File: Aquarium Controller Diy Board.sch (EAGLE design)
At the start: 16 parts

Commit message: 2
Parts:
- added U$1: OLED128X64, Saleem_lib:OLED128X64
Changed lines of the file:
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@@
 <part name="U$10" library="Saleem_lib" deviceset="2PIN" device=""/>
 <part name="U$11" library="Saleem_lib" deviceset="2PIN" device=""/>
+<part name="U$1" library="Saleem_lib" deviceset="OLED128X64" device=""/>
 </parts>
 <sheets>
@@
 <instance part="U$10" gate="G$1" x="139.7" y="17.78"/>
 <instance part="U$11" gate="G$1" x="154.94" y="17.78"/>
+<instance part="U$1" gate="G$1" x="111.76" y="71.12"/>
 </instances>
 <busses>

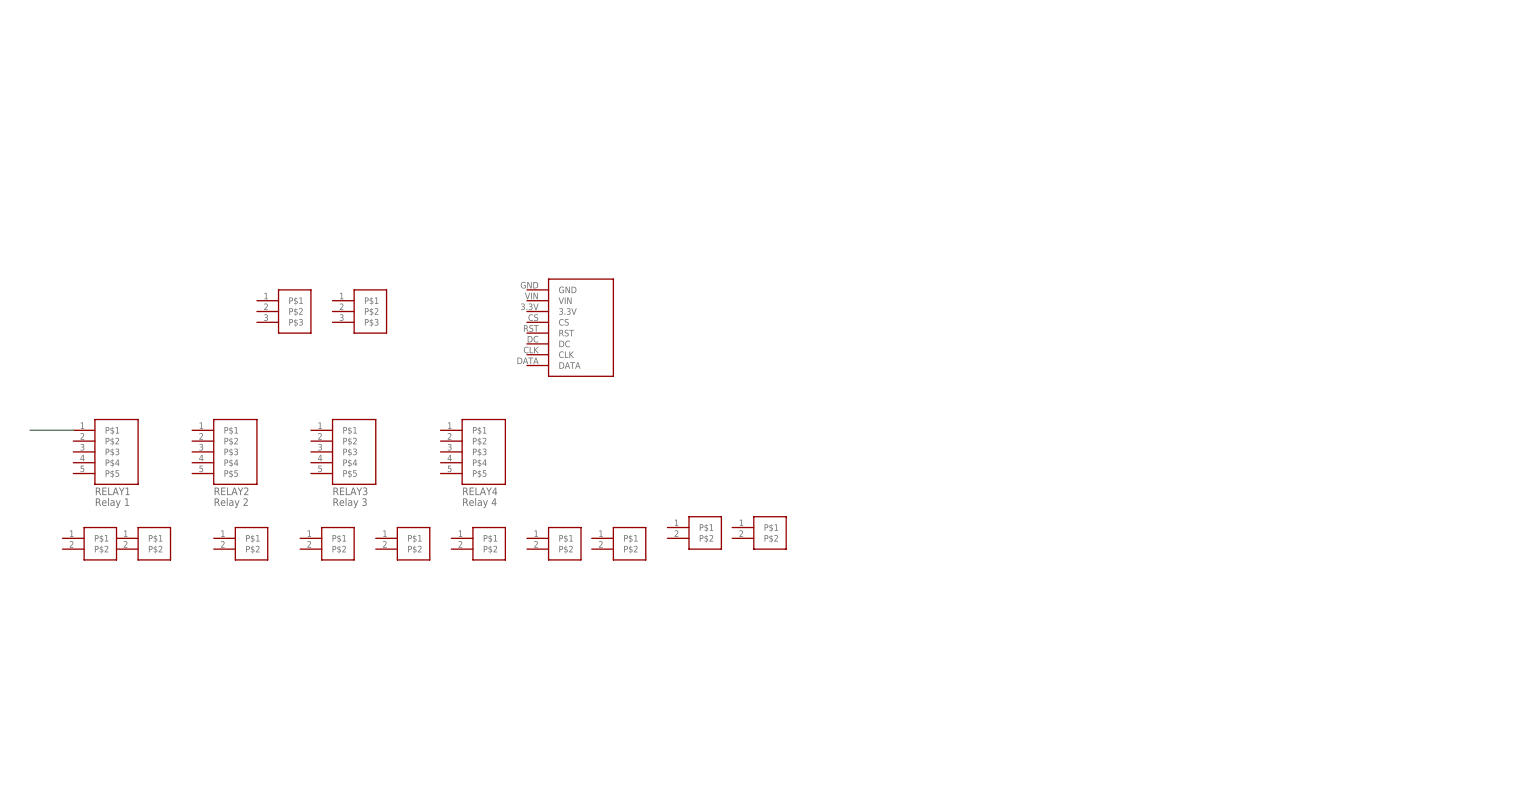
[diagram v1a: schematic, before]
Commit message: still making the schematic and board consistent
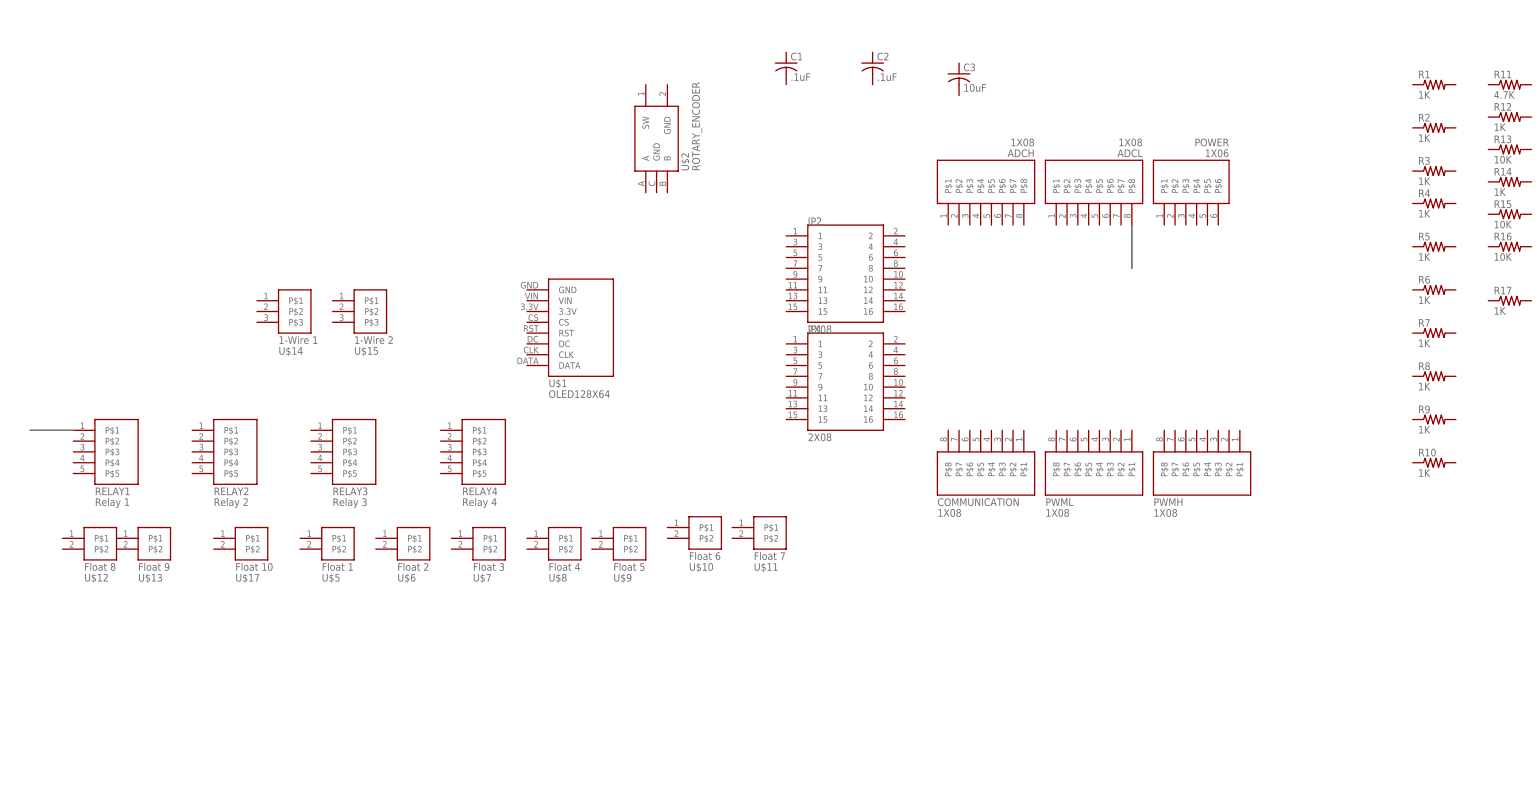
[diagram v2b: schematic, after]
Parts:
- added ADCH, ADCL, COMMUNICATION, PWMH, PWML: 1X08, pinhead:1X08
- added C1, C2: .1uF, resistor:C-USC0805K
- added C3: 10uF, resistor:C-USC0805K
- added JP1, JP2: 2X08, pinhead:2X08
- added POWER: 1X06, pinhead:1X06
- added R1, R10, R12, R14, R17, R2, R3, R4, R5, R6, R7, R8, R9: 1K, rcl:R-US_R0805
- added R11: 4.7K, rcl:R-US_R0805
- added R13, R15, R16: 10K, rcl:R-US_R0805
- added U$2: ROTARY_ENCODER, Saleem_lib:PEC11-4215F-S24
- U$10: value 2PIN -> Float 6
- U$11: value 2PIN -> Float 7
- U$12: value 2PIN -> Float 8
- U$13: value 2PIN -> Float 9
- U$14: value 3PIN -> 1-Wire 1
- U$15: value 3PIN -> 1-Wire 2
- U$17: value 2PIN -> Float 10
- U$5: value 2PIN -> Float 1
- U$6: value 2PIN -> Float 2
- U$7: value 2PIN -> Float 3
- U$8: value 2PIN -> Float 4
- U$9: value 2PIN -> Float 5
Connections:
- new net N$1: ADCL.P$8
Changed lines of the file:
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@@
 <layer number="91" name="Nets" color="2" fill="1" visible="yes" active="yes"/>
 <layer number="92" name="Busses" color="1" fill="1" visible="yes" active="yes"/>
-<layer number="93" name="Pins" color="2" fill="1" visible="no" active="yes"/>
+<layer number="93" name="Pins" color="2" fill="1" visible="yes" active="yes"/>
 <layer number="94" name="Symbols" color="4" fill="1" visible="yes" active="yes"/>
 <layer number="95" name="Names" color="7" fill="1" visible="yes" active="yes"/>
@@
 <layer number="97" name="Info" color="7" fill="1" visible="yes" active="yes"/>
 <layer number="98" name="Guide" color="6" fill="1" visible="yes" active="yes"/>
+<layer number="99" name="SpiceOrder" color="5" fill="1" visible="yes" active="yes"/>
 <layer number="100" name="Mechanical" color="7" fill="1" visible="yes" active="yes"/>
 <layer number="101" name="Patch_Top" color="7" fill="1" visible="yes" active="yes"/>
@@
 </variantdefs>
 <classes>
-<class number="0" name="default" width="0" drill="0">
+<class number="0" name="default" width="0.2032" drill="0.4064">
+<clearance class="0" value="0.2032"/>
+</class>
+<class number="2" name="gnd" width="0.3048" drill="0.7112">
+<clearance class="2" value="0.2032"/>
 </class>
 </classes>
@@
 <part name="RELAY3" library="Saleem_lib" deviceset="5PIN" device="" value="Relay 3"/>
 <part name="RELAY4" library="Saleem_lib" deviceset="5PIN" device="" value="Relay 4"/>
-<part name="U$14" library="Saleem_lib" deviceset="3PIN" device=""/>
-<part name="U$15" library="Saleem_lib" deviceset="3PIN" device=""/>
-<part name="U$12" library="Saleem_lib" deviceset="2PIN" device=""/>
-<part name="U$13" library="Saleem_lib" deviceset="2PIN" device=""/>
-<part name="U$17" library="Saleem_lib" deviceset="2PIN" device=""/>
-<part name="U$5" library="Saleem_lib" deviceset="2PIN" device=""/>
-<part name="U$6" library="Saleem_lib" deviceset="2PIN" device=""/>
-<part name="U$7" library="Saleem_lib" deviceset="2PIN" device=""/>
-<part name="U$8" library="Saleem_lib" deviceset="2PIN" device=""/>
-<part name="U$9" library="Saleem_lib" deviceset="2PIN" device=""/>
-<part name="U$10" library="Saleem_lib" deviceset="2PIN" device=""/>
-<part name="U$11" library="Saleem_lib" deviceset="2PIN" device=""/>
+<part name="U$14" library="Saleem_lib" deviceset="3PIN" device="" value="1-Wire 1"/>
+<part name="U$15" library="Saleem_lib" deviceset="3PIN" device="" value="1-Wire 2"/>
+<part name="U$12" library="Saleem_lib" deviceset="2PIN" device="" value="Float 8"/>
+<part name="U$13" library="Saleem_lib" deviceset="2PIN" device="" value="Float 9"/>
+<part name="U$17" library="Saleem_lib" deviceset="2PIN" device="" value="Float 10"/>
+<part name="U$5" library="Saleem_lib" deviceset="2PIN" device="" value="Float 1"/>
+<part name="U$6" library="Saleem_lib" deviceset="2PIN" device="" value="Float 2"/>
+<part name="U$7" library="Saleem_lib" deviceset="2PIN" device="" value="Float 3"/>
+<part name="U$8" library="Saleem_lib" deviceset="2PIN" device="" value="Float 4"/>
+<part name="U$9" library="Saleem_lib" deviceset="2PIN" device="" value="Float 5"/>
+<part name="U$10" library="Saleem_lib" deviceset="2PIN" device="" value="Float 6"/>
+<part name="U$11" library="Saleem_lib" deviceset="2PIN" device="" value="Float 7"/>
 <part name="U$1" library="Saleem_lib" deviceset="OLED128X64" device=""/>
+<part name="ADCL" library="pinhead" deviceset="1X08" device=""/>
+<part name="ADCH" library="pinhead" deviceset="1X08" device=""/>
+<part name="PWMH" library="pinhead" deviceset="1X08" device=""/>
+<part name="PWML" library="pinhead" deviceset="1X08" device=""/>
+<part name="COMMUNICATION" library="pinhead" deviceset="1X08" device=""/>
+<part name="JP2" library="pinhead" deviceset="2X08" device=""/>
+<part name="JP1" library="pinhead" deviceset="2X08" device=""/>
+<part name="POWER" library="pinhead" deviceset="1X06" device=""/>
+<part name="U$2" library="Saleem_lib" deviceset="PEC11-4215F-S24" device="" value="ROTARY_ENCODER"/>
+<part name="C1" library="resistor" deviceset="C-US" device="C0805K" value=".1uF"/>
+<part name="C2" library="resistor" deviceset="C-US" device="C0805K" value=".1uF"/>
+<part name="C3" library="resistor" deviceset="C-US" device="C0805K" value="10uF"/>
+<part name="R1" library="rcl" deviceset="R-US_" device="R0805" value="1K"/>
+<part name="R2" library="rcl" deviceset="R-US_" device="R0805" value="1K"/>
+<part name="R3" library="rcl" deviceset="R-US_" device="R0805" value="1K"/>
+<part name="R4" library="rcl" deviceset="R-US_" device="R0805" value="1K"/>
+<part name="R5" library="rcl" deviceset="R-US_" device="R0805" value="1K"/>
+<part name="R6" library="rcl" deviceset="R-US_" device="R0805" value="1K"/>
+<part name="R7" library="rcl" deviceset="R-US_" device="R0805" value="1K"/>
+<part name="R8" library="rcl" deviceset="R-US_" device="R0805" value="1K"/>
+<part name="R9" library="rcl" deviceset="R-US_" device="R0805" value="1K"/>
+<part name="R10" library="rcl" deviceset="R-US_" device="R0805" value="1K"/>
+<part name="R11" library="rcl" deviceset="R-US_" device="R0805" value="4.7K"/>
+<part name="R12" library="rcl" deviceset="R-US_" device="R0805" value="1K"/>
+<part name="R13" library="rcl" deviceset="R-US_" device="R0805" value="10K"/>
+<part name="R14" library="rcl" deviceset="R-US_" device="R0805" value="1K"/>
+<part name="R15" library="rcl" deviceset="R-US_" device="R0805" value="10K"/>
+<part name="R16" library="rcl" deviceset="R-US_" device="R0805" value="10K"/>
+<part name="R17" library="rcl" deviceset="R-US_" device="R0805" value="1K"/>
 </parts>
 <sheets>
@@
 <instance part="U$11" gate="G$1" x="154.94" y="17.78"/>
 <instance part="U$1" gate="G$1" x="111.76" y="71.12"/>
+<instance part="ADCL" gate="G$1" x="228.6" y="101.6" rot="R90"/>
+<instance part="ADCH" gate="G$1" x="203.2" y="101.6" rot="R90"/>
+<instance part="PWMH" gate="G$1" x="256.54" y="33.02" rot="R270"/>
+<instance part="PWML" gate="G$1" x="231.14" y="33.02" rot="R270"/>
+<instance part="COMMUNICATION" gate="G$1" x="205.74" y="33.02" rot="R270"/>
+<instance part="JP2" gate="G$1" x="167.64" y="81.28"/>
+<instance part="JP1" gate="G$1" x="167.64" y="55.88"/>
+<instance part="POWER" gate="G$1" x="251.46" y="101.6" rot="R90"/>
+<instance part="U$2" gate="G$1" x="127" y="111.76"/>
+<instance part="C1" gate="G$1" x="157.48" y="129.54"/>
+<instance part="C2" gate="G$1" x="177.8" y="129.54"/>
+<instance part="C3" gate="G$1" x="198.12" y="127"/>
+<instance part="R1" gate="G$1" x="309.88" y="124.46"/>
+<instance part="R2" gate="G$1" x="309.88" y="114.3"/>
+<instance part="R3" gate="G$1" x="309.88" y="104.14"/>
+<instance part="R4" gate="G$1" x="309.88" y="96.52"/>
+<instance part="R5" gate="G$1" x="309.88" y="86.36"/>
+<instance part="R6" gate="G$1" x="309.88" y="76.2"/>
+<instance part="R7" gate="G$1" x="309.88" y="66.04"/>
+<instance part="R8" gate="G$1" x="309.88" y="55.88"/>
+<instance part="R9" gate="G$1" x="309.88" y="45.72"/>
+<instance part="R10" gate="G$1" x="309.88" y="35.56"/>
+<instance part="R11" gate="G$1" x="327.66" y="124.46"/>
+<instance part="R12" gate="G$1" x="327.66" y="116.84"/>
+<instance part="R13" gate="G$1" x="327.66" y="109.22"/>
+<instance part="R14" gate="G$1" x="327.66" y="101.6"/>
+<instance part="R15" gate="G$1" x="327.66" y="93.98"/>
+<instance part="R16" gate="G$1" x="327.66" y="86.36"/>
+<instance part="R17" gate="G$1" x="327.66" y="73.66"/>
 </instances>
 <busses>
@@
 </segment>
 </net>
+<net name="N$1" class="0">
+<segment>
+<pinref part="ADCL" gate="G$1" pin="P$8"/>
+<wire x1="238.76" y1="91.44" x2="238.76" y2="81.28" width="0.1524" layer="91"/>
+</segment>
+</net>

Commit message: 2
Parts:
- C1: device resistor:C-USC0805K -> rcl:C-USC0805K
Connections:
- new net 1WIRE_DQ: JP1.3, R11.2
- new net 5V: POWER.P$3, R1.2, R10.1, R11.1, R13.2, R15.2, R16.2, R2.1, R3.1, R4.1, R5.1, R6.1, R7.1, R8.1, R9.1
- new net A: R12.1, R13.1
- new net B: R14.2, R15.1
- new net CLK: PWML.P$3
- new net CS: PWML.P$6
- new net DATA: JP1.6
- new net DC: PWML.P$4
- new net F1: R1.1
- new net F10: PWMH.P$1, R10.2
- new net F2: R2.2
- new net F3: JP1.15, R3.2
- new net F4: JP1.16, R4.2
- new net F5: COMMUNICATION.P$2, R5.2
- new net F6: COMMUNICATION.P$1, R6.2
- new net F7: PWML.P$8, R7.2
- new net F8: PWML.P$7, R8.2
- new net F9: PWMH.P$2, R9.2
- new net GND: C1.2, C2.2, C3.2, POWER.P$4, POWER.P$5, PWMH.P$7, RELAY1.P$5, RELAY2.P$5, RELAY3.P$5, RELAY4.P$5, U$10.P$2, U$11.P$2, U$12.P$2, U$13.P$2, U$17.P$2, U$2.GND@1, U$2.GND@2, U$5.P$2, U$6.P$2, U$7.P$2, U$8.P$2, U$9.P$2
- new net IN1-1: JP2.1, RELAY1.P$4
- new net IN1-2: JP2.3, RELAY1.P$3
- new net IN1-3: JP2.5, RELAY1.P$2
- new net IN2-1: JP2.8, RELAY2.P$4
- new net IN2-2: JP2.6, RELAY2.P$3
- new net IN2-3: JP2.4, RELAY2.P$2
- new net IN2-4: JP2.2, RELAY2.P$1
- new net IN3-1: JP2.15, RELAY3.P$4
- new net IN3-2: JP2.13, RELAY3.P$3
- new net IN3-3: JP2.11, RELAY3.P$2
- new net IN3-4: JP2.9, RELAY3.P$1
- new net IN4-1: JP2.10, RELAY4.P$4
- new net IN4-2: JP2.12, RELAY4.P$3
- new net IN4-3: JP2.14, RELAY4.P$2
- new net IN4-4: JP2.16, RELAY4.P$1
- new net RST: PWML.P$5
- new net S1: C3.1, PWMH.P$3, R17.1
- new net TERMA: C2.1, PWMH.P$4, R12.2
- new net TERMB: C1.1, PWMH.P$5, R14.1
- net IN1-4: now also JP2.7
- net N$1: now also R16.1, R17.2; no longer ADCL.P$8
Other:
- moved on the sheet: ADCH, ADCL, COMMUNICATION, POWER, PWMH, R1, R11, R12, R13, R14, R15, R16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

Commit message: 4
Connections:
- net 1WIRE_DQ: now also U$14.P$2, U$15.P$2
- net 5V: now also U$1.VIN, U$14.P$1, U$15.P$1
- net A: now also U$2.A
- net B: now also U$2.B
- net CLK: now also U$1.CLK
- net CS: now also U$1.CS
- net DATA: now also U$1.DATA
- net DC: now also U$1.DC
- net F1: now also U$5.P$1
- net F10: now also U$17.P$1
- net F2: now also U$6.P$1
- net F3: now also U$7.P$1
- net F4: now also U$8.P$1
- net F5: now also U$9.P$1
- net F6: now also U$10.P$1
- net F7: now also U$11.P$1
- net F8: now also U$12.P$1
- net F9: now also U$13.P$1
- net GND: now also U$1.GND, U$14.P$3, U$15.P$3
- net N$1: now also U$2.SW
- net RST: now also U$1.RST
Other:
- moved on the sheet: U$14, U$15
